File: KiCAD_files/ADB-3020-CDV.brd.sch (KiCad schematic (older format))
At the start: 113 parts, among them IC1 7812T, IC2 NE5532N, IC3 LM2576, IC4 NE555, IC5 IR2184D, J1 + IN, J2 - IN, J3 + OUT, J4 PIN2F061.040, J5 + IN, J6 - IN, J7 PIN2F061.040, J8 - OUT, Q1 IRFP240-H, Q2 IRFP240-H, Q4 BDX53, T1 BC337, T2 BC337

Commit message: Added footprints
To do before merge:
* review the footprints
* draw inductors footprints 
* draw J1 to J8 footprints (faston tabs)
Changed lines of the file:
@@
 $EndComp
 Wire Wire Line
-	3400 4100 3800 4100
+	3400 4100 3500 4100
+Wire Wire Line
+	3500 4100 3700 4100
+Wire Wire Line
+	3700 4100 3800 4100
 Connection ~ 5800 6300
 Connection ~ 5400 6300
@@
 Connection ~ 4400 4700
 Wire Wire Line
-	4300 4700 4700 4700
+	4300 4700 4400 4700
+Wire Wire Line
+	4400 4700 4700 4700
 Connection ~ 6100 700
 Connection ~ 5800 4400
 Connection ~ 5600 4400
 Wire Wire Line
-	5600 4400 5900 4400
+	5600 4400 5800 4400
+Wire Wire Line
+	5800 4400 5900 4400
 Wire Wire Line
 	5600 4300 5600 4400
@@
 Connection ~ 6100 1100
 Wire Wire Line
-	6100 700  6100 1200
+	6100 700  6100 1100
+Wire Wire Line
+	6100 1100 6100 1200
 Wire Wire Line
 	5900 1100 5900 1200
 Wire Wire Line
-	5900 1100 6200 1100
-Wire Wire Line
-	6000 700  6300 700
+	5900 1100 6100 1100
+Wire Wire Line
+	6100 1100 6200 1100
+Wire Wire Line
+	6000 700  6100 700
+Wire Wire Line
+	6100 700  6300 700
 Connection ~ 4700 1600
 Connection ~ 5300 1100
@@
 	4700 2000 9600 2000
 Wire Wire Line
-	4700 1100 4700 2000
-Wire Wire Line
-	4400 1100 5300 1100
+	4700 1100 4700 1600
+Wire Wire Line
+	4700 1600 4700 2000
+Wire Wire Line
+	4400 1100 4700 1100
+Wire Wire Line
+	4700 1100 5300 1100
 Wire Wire Line
 	4396 909  4400 1100
@@
 	9100 3600 9100 3200
 Wire Wire Line
-	9600 3600 8800 3600
+	9600 3600 9100 3600
+Wire Wire Line
+	9100 3600 8800 3600
 Connection ~ 8800 3200
 Wire Wire Line
@@
 	3500 4200 3500 4100
 Wire Wire Line
-	3700 3950 3700 4200
+	3700 3950 3700 4100
+Wire Wire Line
+	3700 4100 3700 4200
 Connection ~ 2900 3800
 Wire Wire Line
-	2900 3600 2900 3900
+	2900 3600 2900 3800
+Wire Wire Line
+	2900 3800 2900 3900
 Wire Wire Line
 	3800 6400 3800 6200
@@
 	4600 2700 4600 2800
 Wire Wire Line
-	4000 2700 5000 2700
-Wire Wire Line
-	4200 2500 4200 2800
+	4000 2700 4200 2700
+Wire Wire Line
+	4200 2700 4400 2700
+Wire Wire Line
+	4400 2700 4600 2700
+Wire Wire Line
+	4600 2700 4800 2700
+Wire Wire Line
+	4800 2700 5000 2700
+Wire Wire Line
+	4200 2500 4200 2700
+Wire Wire Line
+	4200 2700 4200 2800
 Connection ~ 7700 2600
 Connection ~ 7700 2800
 Wire Wire Line
-	7700 2400 7700 3200
+	7700 2400 7700 2600
+Wire Wire Line
+	7700 2600 7700 2800
+Wire Wire Line
+	7700 2800 7700 3200
 Wire Wire Line
 	8100 2800 7700 2800
 Connection ~ 7100 3900
 Wire Wire Line
-	7100 3800 7100 4000
+	7100 3800 7100 3900
+Wire Wire Line
+	7100 3900 7100 4000
 Wire Wire Line
 	6700 3900 7100 3900
@@
 	7200 1100 7200 1200
 Wire Wire Line
-	6800 1100 8200 1100
+	6800 1100 6900 1100
+Wire Wire Line
+	6900 1100 7200 1100
+Wire Wire Line
+	7200 1100 7400 1100
+Wire Wire Line
+	7400 1100 7600 1100
+Wire Wire Line
+	7600 1100 7800 1100
+Wire Wire Line
+	7800 1100 8200 1100
 Wire Wire Line
 	8200 1100 8200 900
@@
 	5300 1800 5700 1800
 Wire Wire Line
-	1600 1500 5300 1500
+	2300 1500 2500 1500
+Wire Wire Line
+	2500 1500 2700 1500
+Wire Wire Line
+	2700 1500 2900 1500
+Wire Wire Line
+	2900 1500 3100 1500
+Wire Wire Line
+	3100 1500 3300 1500
+Wire Wire Line
+	3300 1500 3500 1500
+Wire Wire Line
+	3500 1500 3700 1500
+Wire Wire Line
+	3700 1500 3900 1500
+Wire Wire Line
+	3900 1500 5300 1500
 Wire Wire Line
 	1600 1700 1600 1500
 Wire Wire Line
-	5300 1500 5300 1800
+	5300 1500 5300 1600
+Wire Wire Line
+	5300 1600 5300 1800
 Connection ~ 9900 5500
 Wire Wire Line
 	10400 5500 9900 5500
 Wire Wire Line
-	9900 5300 9900 5600
+	9900 5300 9900 5500
+Wire Wire Line
+	9900 5500 9900 5600
 Connection ~ 10700 4700
 Wire Wire Line
 	10300 4300 10700 4300
 Wire Wire Line
-	10700 4300 10700 5400
+	10700 4300 10700 4700
+Wire Wire Line
+	10700 4700 10700 5400
 Connection ~ 4900 1600
 Connection ~ 5100 1400
@@
 	4900 1400 5100 1400
 Wire Wire Line
-	4900 1400 4900 1900
+	4900 1400 4900 1600
+Wire Wire Line
+	4900 1600 4900 1900
 Wire Wire Line
 	9700 4000 9700 2700
@@
 	2300 1200 2300 1100
 Wire Wire Line
-	1600 1100 4000 1100
+	1600 1100 2300 1100
+Wire Wire Line
+	2300 1100 2500 1100
+Wire Wire Line
+	2500 1100 2700 1100
+Wire Wire Line
+	2700 1100 2900 1100
+Wire Wire Line
+	2900 1100 3100 1100
+Wire Wire Line
+	3100 1100 3300 1100
+Wire Wire Line
+	3300 1100 3500 1100
+Wire Wire Line
+	3500 1100 3700 1100
+Wire Wire Line
+	3700 1100 3900 1100
+Wire Wire Line
+	3900 1100 4000 1100
 Wire Wire Line
 	1600 900  1600 1100
@@
 	8200 1500 8200 1700
 Wire Wire Line
-	5700 1500 8200 1500
+	5700 1500 5900 1500
+Wire Wire Line
+	5900 1500 6100 1500
+Wire Wire Line
+	6100 1500 6900 1500
+Wire Wire Line
+	6900 1500 7200 1500
+Wire Wire Line
+	7200 1500 7400 1500
+Wire Wire Line
+	7400 1500 7600 1500
+Wire Wire Line
+	7600 1500 7800 1500
+Wire Wire Line
+	7800 1500 8200 1500
 Wire Wire Line
 	5700 1600 5700 1500
@@
 	7500 3600 7700 3600
 Wire Wire Line
-	7500 3600 7500 5600
+	7500 3600 7500 4800
+Wire Wire Line
+	7500 4800 7500 5600
 Connection ~ 7100 4800
 Wire Wire Line
@@
 	6200 6400 6200 5200
 Wire Wire Line
-	5800 5200 6300 5200
+	5800 5200 6200 5200
+Wire Wire Line
+	6200 5200 6300 5200
 Wire Wire Line
 	6100 6400 6200 6400
@@
 	5500 6400 5500 6600
 Wire Wire Line
-	5800 6200 5800 6400
+	5800 6200 5800 6300
+Wire Wire Line
+	5800 6300 5800 6400
 Connection ~ 5400 6400
 Wire Wire Line
-	5400 6200 5400 6600
+	5400 6200 5400 6300
+Wire Wire Line
+	5400 6300 5400 6400
+Wire Wire Line
+	5400 6400 5400 6600
 Wire Wire Line
 	2700 5600 2300 5600
@@
 	3800 5400 4000 5400
 Wire Wire Line
-	3900 5700 4100 5700
+	3900 5700 4000 5700
+Wire Wire Line
+	4000 5700 4100 5700
 Wire Wire Line
 	4700 4700 4700 5500
@@
 	2000 4500 1800 4500
 Wire Wire Line
-	2000 3800 2000 4500
+	2000 3800 2000 4400
+Wire Wire Line
+	2000 4400 2000 4500
 Wire Wire Line
 	2100 3800 2000 3800
@@
 	4300 2100 9400 2100
 Wire Wire Line
-	4300 1300 4300 2100
+	4300 1300 4300 1600
+Wire Wire Line
+	4300 1600 4300 2100
 Wire Wire Line
 	9400 2100 9400 2300
@@
 	5800 3500 5800 3200
 Wire Wire Line
-	5600 3500 6200 3500
+	5600 3500 5800 3500
+Wire Wire Line
+	5800 3500 6200 3500
 Wire Wire Line
 	5600 3300 5600 3500
@@
 	2600 5900 2600 6800
 Wire Wire Line
-	2300 5900 2700 5900
+	2300 5900 2600 5900
+Wire Wire Line
+	2600 5900 2700 5900
 Connection ~ 4200 5300
 Wire Wire Line
@@
 	5600 3000 5800 3000
 Wire Wire Line
-	2700 2700 3200 2700
+	2700 2700 2800 2700
+Wire Wire Line
+	2800 2700 3000 2700
+Wire Wire Line
+	3000 2700 3200 2700
 Wire Wire Line
 	2800 2700 2800 2800
@@
 	10200 4300 9900 4300
 Wire Wire Line
-	9900 4300 9900 4900
-Wire Wire Line
-	9800 4700 10000 4700
+	9900 4300 9900 4700
+Wire Wire Line
+	9900 4700 9900 4900
+Wire Wire Line
+	9800 4700 9900 4700
+Wire Wire Line
+	9900 4700 10000 4700
 NoConn ~ 2900 4300
 Wire Wire Line
@@
 	5600 2800 5600 3000
 Wire Wire Line
-	3000 2600 3000 2800
+	3000 2600 3000 2700
+Wire Wire Line
+	3000 2700 3000 2800
 Connection ~ 3000 2700
 $Comp
@@
 	1    0    0    -1
 $EndComp
+Wire Wire Line
+	1600 1500 2300 1500
 $EndSCHEMATC

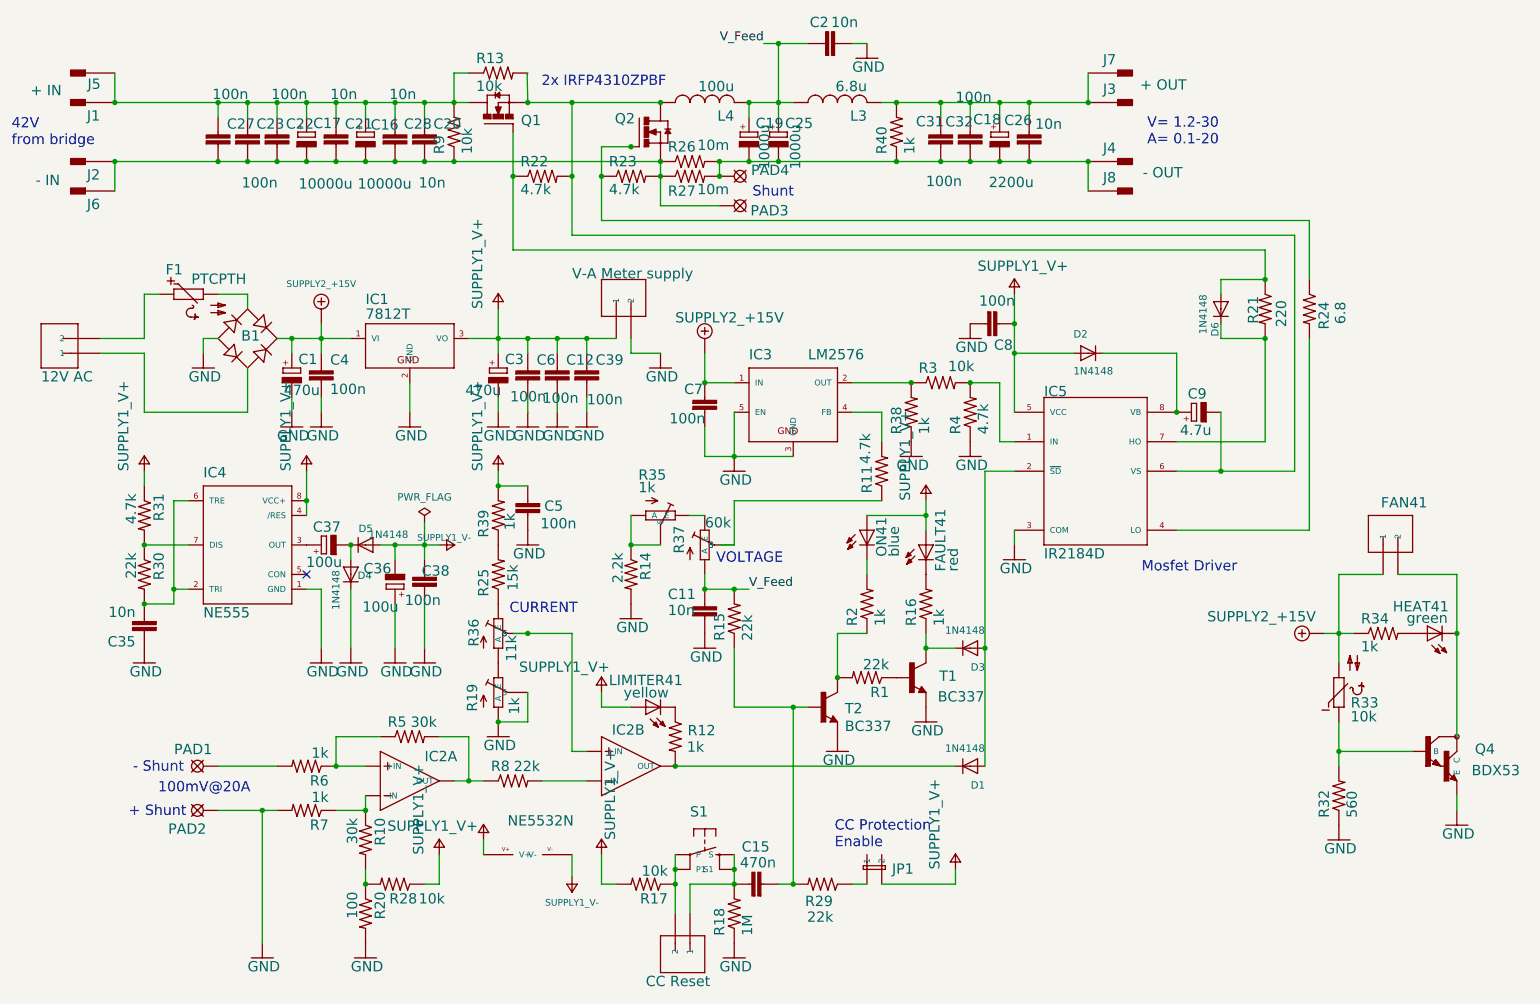
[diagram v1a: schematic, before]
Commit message: Almost finished layout and fixes.
* fixed fp-lib-table
* fixed schematic

Missing:
* faston footprints
* faston in layout

Requires review
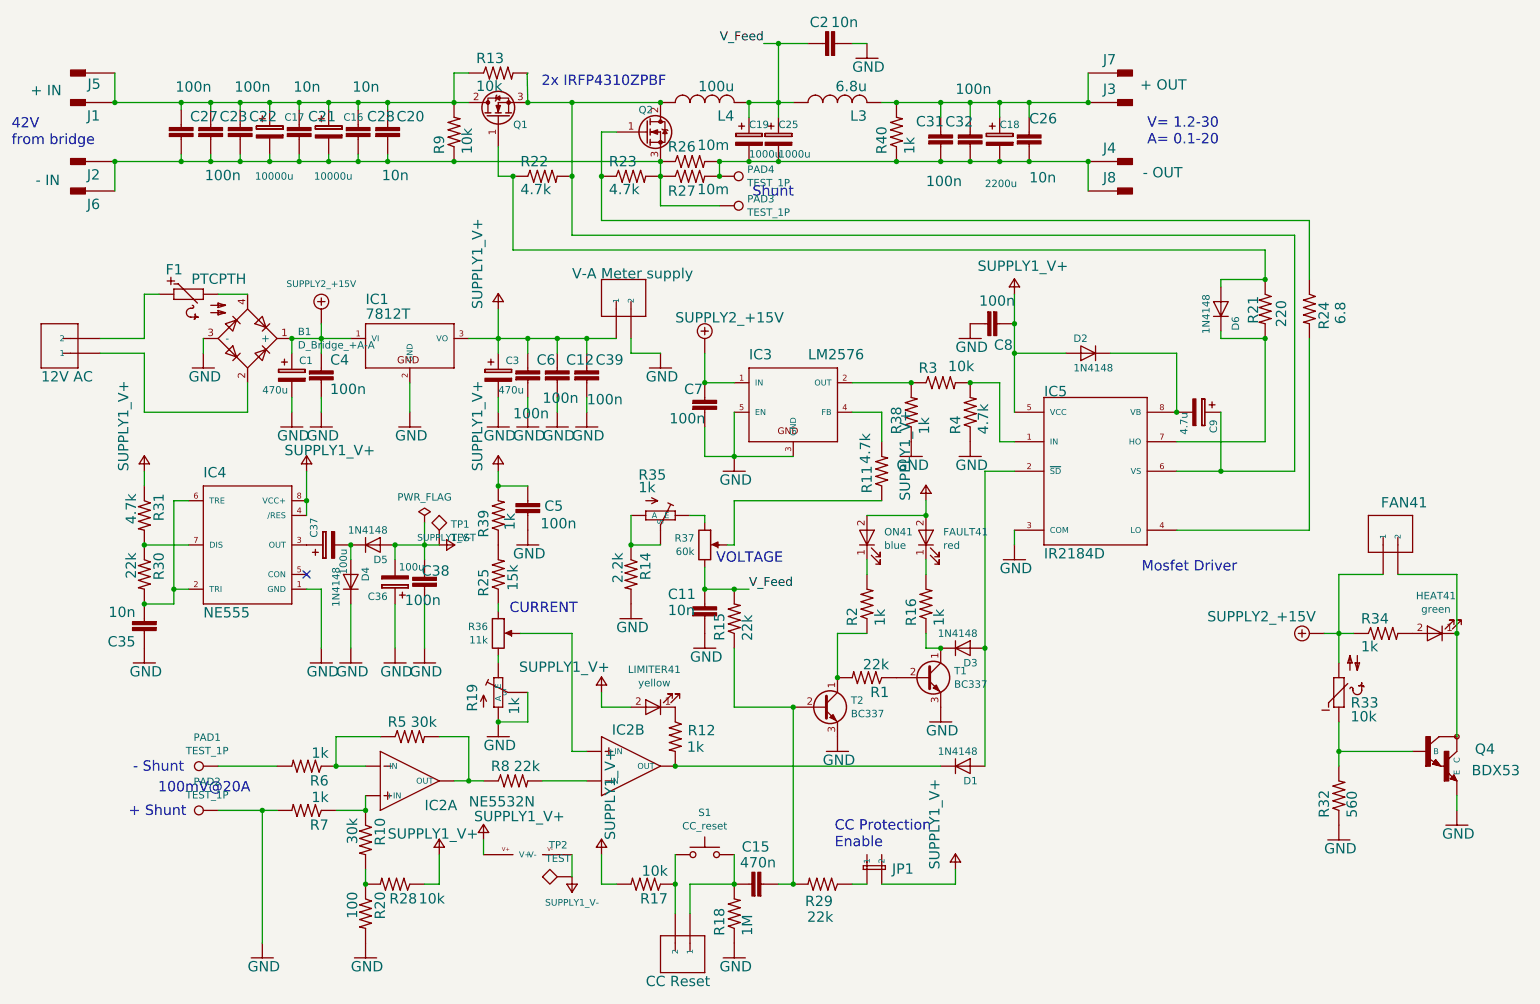
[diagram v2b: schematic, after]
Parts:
- removed B1: RECTIFIER-RB1A, RECTIFIER_RB1A, symbol RECTIFIER_RECTIFIER-RB1A
- removed C1, C3: 470u, RCL_E2-5, symbol RCL_CPOL-EUE2-5
- removed C16, C17: 10000u, RCL_E2-5, symbol RCL_CPOL-EUE2-5
- removed C18: 2200u, RCL_E2-5, symbol RCL_CPOL-EUE2-5
- removed C19, C25: 1000u, RCL_E2-5, symbol RCL_CPOL-EUE2-5
- removed C36, C37: 100u, RCL_E2-5, symbol RCL_CPOL-EUE2-5
- removed C9: 4.7u, RCL_E2-5, symbol RCL_CPOL-EUE2-5
- removed D1, D2, D3, D4, D5, D6: 1N4148, ADAFRUIT_DO-1N4148, symbol ADAFRUIT_DIODEDO-1N4148
- removed FAULT41: red, ADAFRUIT_LED3MM, symbol ADAFRUIT_LED3MM
- removed HEAT41: green, ADAFRUIT_LED3MM, symbol ADAFRUIT_LED3MM
- removed LIMITER41: yellow, ADAFRUIT_LED3MM, symbol ADAFRUIT_LED3MM
- removed ON41: blue, ADAFRUIT_LED3MM, symbol ADAFRUIT_LED3MM
- removed PAD1, PAD2, PAD3, PAD4: LSP13, SOLPAD_LSP13, symbol SOLPAD_LSP13
- removed Q1, Q2: IRFP240-H, TRANSISTOR-POWER_TO247BH, symbol TRANSISTOR-POWER_IRFP240-H
- removed R36: 11k, POT_S64YW, symbol POT_TRIM_1234-S64YW
- removed R37: 60k, POT_S64YW, symbol POT_TRIM_1234-S64YW
- removed S1: CC Reset, ADAFRUIT_B3F-40XX, symbol ADAFRUIT_40-XX
- removed T1, T2: BC337, TRANSISTOR_TO92, symbol TRANSISTOR_BC337
- added B1: D_Bridge_+A-A, Diodes_THT:Diode_Bridge_Round_D9.8mm, symbol D_Bridge_+A-A
- added C1, C3: 470u, Capacitors_THT:CP_Radial_D10.0mm_P5.00mm, symbol CP
- added C16, C17: 10000u, Capacitors_THT:CP_Radial_D30.0mm_P10.00mm_SnapIn, symbol CP
- added C18: 2200u, Capacitors_THT:CP_Radial_D18.0mm_P7.50mm, symbol CP
- added C19, C25: 1000u, Capacitors_THT:CP_Radial_D16.0mm_P7.50mm, symbol CP
- added C36, C37: 100u, Capacitors_THT:CP_Radial_D6.3mm_P2.50mm, symbol CP
- added C9: 4.7u, Capacitors_THT:CP_Radial_D5.0mm_P2.00mm, symbol CP
- added D1, D2, D3: 1N4148, Diodes_THT:D_DO-35_SOD27_P10.16mm_Horizontal, symbol D
- added D4, D5: 1N4148, Diodes_THT:D_DO-35_SOD27_P7.62mm_Horizontal, symbol D
- added D6: 1N4148, Diodes_THT:D_DO-35_SOD27_P12.70mm_Horizontal, symbol D
- added FAULT41: red, LEDs:LED_D3.0mm, symbol LED
- added HEAT41: green, LEDs:LED_D3.0mm, symbol LED
- added LIMITER41: yellow, LEDs:LED_D3.0mm, symbol LED
- added ON41: blue, LEDs:LED_D3.0mm, symbol LED
- added PAD1, PAD2, PAD3, PAD4: TEST_1P, Wire_Pads:SolderWirePad_single_1mmDrill, symbol TEST_1P
- added Q1, Q2: IRFP4310ZPBF, TO_SOT_Packages_THT:TO-247_TO-3P_Horizontal, symbol Q_NMOS_GDS
- added R36: 11k, Potentiometers:Potentiometer_Trimmer_ACP_CA9v_Horizontal_Px10.0mm_Py5.0mm, symbol POT
- added R37: 60k, Potentiometers:Potentiometer_Trimmer_ACP_CA9v_Horizontal_Px10.0mm_Py5.0mm, symbol POT
- added S1: CC_reset, Buttons_Switches_THT:SW_PUSH_6mm, symbol SW_Push
- added T1, T2: BC337, TO_SOT_Packages_THT:TO-92_Molded_Narrow, symbol Q_NPN_CBE
- added TP1, TP2: TEST, Wire_Pads:SolderWirePad_single_1mmDrill, symbol TEST
- C11, C12, C15, C2, C35, C38, C39, C4, C5, C6, C7, C8: footprint CAPACITOR-WIMA_C2.5-2 -> Capacitors_SMD:C_0805
- C20, C21, C22, C23, C26, C27, C28, C31, C32: footprint CAPACITOR-WIMA_C2.5-2 -> Capacitors_SMD:C_1206
- F1: footprint PTC-NTC_P660 -> Resistors_THT:R_Axial_DIN0204_L3.6mm_D1.6mm_P5.08mm_Horizontal
- FAN41, LOGIC_POWER41: footprint CON-AMP-QUICK_02PA -> Connectors_Phoenix:PhoenixContact_MCV-G_02x5.08mm_Vertical
- IC1: footprint ADAFRUIT_TO220H -> TO_SOT_Packages_THT:TO-220_Vertical
- IC2: footprint LINEAR_DIL08 -> Housings_DIP:DIP-8_W7.62mm_LongPads
- IC3: footprint LINEAR_TO220-52 -> TO_SOT_Packages_THT:TO-220-5_Pentawatt_Multiwatt-5_Vertical_StaggeredType1
- IC4: footprint ST-MICROELECTRONICS_DIL-08 -> Housings_DIP:DIP-8_W7.62mm_LongPads
- IC5: footprint IRS_DIL08 -> Housings_DIP:DIP-8_W7.62mm_LongPads
- J1, J2, J3, J4, J5, J6, J7, J8: footprint CON-FASTON_F061.040 -> (none)
- JP1: footprint JUMPER_JP1 -> Pin_Headers:Pin_Header_Straight_1x02_Pitch2.54mm
- L3: footprint ADAFRUIT_6000 -> customparts:smallinductor
- L4: footprint ADAFRUIT_6000 -> customparts:biginductor
- Q4: footprint TRANSISTOR_TO220 -> TO_SOT_Packages_THT:TO-126_Vertical
- R1, R10, R11, R12, R14, R16, R17, R18, R2, R20, R25, R28, R29, R30, R31, R32, R34, R39, R4, R5, R7, R8: footprint ADAFRUIT_0204_5 -> Resistors_THT:R_Axial_DIN0204_L3.6mm_D1.6mm_P5.08mm_Horizontal
- R13, R22, R23, R38, R9: footprint ADAFRUIT_0204_5 -> Resistors_THT:R_Axial_DIN0207_L6.3mm_D2.5mm_P10.16mm_Horizontal
- R15, R3, R6: footprint ADAFRUIT_0204_5 -> Resistors_THT:R_Axial_DIN0204_L3.6mm_D1.6mm_P7.62mm_Horizontal
- R19, R35: footprint ADAFRUIT_TRIM-3386 -> Potentiometers:Potentiometer_Trimmer_Bourns_3296Y
- R21, R24: footprint ADAFRUIT_0204_5 -> Resistors_THT:R_Axial_DIN0207_L6.3mm_D2.5mm_P15.24mm_Horizontal
- R26, R27: footprint ADAFRUIT_0204_5 -> Resistors_SMD:R_2512
- R33: footprint PTC-NTC_P640 -> Resistors_THT:R_Axial_DIN0204_L3.6mm_D1.6mm_P2.54mm_Vertical
- R40: footprint ADAFRUIT_0204_5 -> Resistors_THT:R_Axial_DIN0309_L9.0mm_D3.2mm_P12.70mm_Horizontal
- RESET41, V-A_METER_SUPPLY41: footprint CON-AMP-QUICK_02PA -> Pin_Headers:Pin_Header_Straight_1x02_Pitch2.54mm
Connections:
- net +15V: now also B1.1 (+), C1.1
- net GND: now also B1.3 (-), C1.2, C3.2, C36.1, D4.1 (K), PAD2.1, T1.3 (E), T2.3 (E)
- net V+: now also C3.1, D2.2 (A), FAULT41.2 (A), LIMITER41.2 (A), ON41.2 (A)
- net V-: now also C36.2, D5.2 (A), TP1.1, TP2.1
- net V_Feed: now also C19.1, C25.1, R37.3
- net at F1.2: now also B1.4
- net at LOGIC_POWER41.1: now also B1.2
- net at IC5.8 (VB): now also C9.2, D2.1 (K)
- net at IC5.6 (VS), L4.1, R13.2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: now also C9.1, Q1.3 (S), Q2.2 (D)
- net at C15.1, R18.2, RESET41.1: now also S1.2
- net at C15.2, R15.1, R29.2: now also T2.2 (B)
- net at C20.1, C21.1, C22.1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: now also C16.1, C17.1, Q1.2 (D)
- net at C20.2, C21.2, C22.2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: now also C16.2, C17.2, PAD3.1, Q2.3 (S)
- net at C26.1, C31.1, C32.1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: now also C18.1
- net at C26.2, C31.2, C32.2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: now also C18.2, C19.2, C25.2, PAD4.1
- net at IC4.3 (OUT): now also C37.1
- net at IC5.2 (~SD): now also D1.2 (A), D3.2 (A)
- net at IC2.7 (OUT), R12.2: now also D1.1 (K)
- net at R16.1: now also D3.1 (K), T1.1 (C)
- net at R21.1, R22.1: now also D6.2 (A), Q1.1 (G)
- net at IC5.7 (HO), R21.2: now also D6.1 (K)
- net at FAN41.2, Q4.2 (C): now also HEAT41.1 (K)
- net at R16.2: now also FAULT41.1 (K)
- net at R34.2: now also HEAT41.2 (A)
- net at R10.1, R7.1: now also IC2.3 (+IN); no longer IC2.2 (-IN)
- net at R5.1, R6.1: now also IC2.2 (-IN); no longer IC2.3 (+IN)
- net at IC2.5 (+IN): now also R36.2
- net at R12.1: now also LIMITER41.1 (K)
- net at R2.2: now also ON41.1 (K)
- net at R6.2: now also PAD1.1
- net at R23.1, R24.1: now also Q2.1 (G)
- net at R1.1: now also T1.2 (B)
- net at R1.2, R2.1: now also T2.1 (C)
- net at R11.1: now also R37.2
- net at R17.1, RESET41.2: now also S1.1
- net at R19.3 (E): now also R36.3
- net at R25.1: now also R36.1
- net at R35.3 (E): now also R37.1
- new net: C37.2, D4.2 (A), D5.1 (K)
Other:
- moved on the sheet: C20, C21, C22, C23, C27, C28
